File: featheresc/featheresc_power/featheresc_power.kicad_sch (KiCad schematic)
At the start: 19 parts, among them J1 VIN_GND, J2 VIN_POS, J7 interconnect1, J8 interconnect2

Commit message: Power board: update terminals, many minor tweaks
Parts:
- J1, J2: footprint featheresc:screw_lug_terminal -> featheresc:screwterminal_temile_MFR04425
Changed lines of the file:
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@@
     (date "2021-11-20")
   )
+  (junction (at 114.3 94.615) (diameter 0) (color 0 0 0 0))
+  (junction (at 110.49 76.835) (diameter 0) (color 0 0 0 0))
+  (junction (at 73.025 94.615) (diameter 0) (color 0 0 0 0))
   (junction (at 126.365 76.835) (diameter 0) (color 0 0 0 0))
-  (junction (at 122.555 76.835) (diameter 0) (color 0 0 0 0))
-  (junction (at 110.49 94.615) (diameter 0) (color 0 0 0 0))
+  (junction (at 109.22 101.6) (diameter 0) (color 0 0 0 0))
+  (junction (at 114.3 101.6) (diameter 0) (color 0 0 0 0))
+  (junction (at 122.555 58.42) (diameter 0) (color 0 0 0 0))
+  (junction (at 82.55 76.835) (diameter 0) (color 0 0 0 0))
   (junction (at 80.645 101.6) (diameter 0) (color 0 0 0 0))
   (junction (at 109.22 106.68) (diameter 0) (color 0 0 0 0))
-  (junction (at 114.3 101.6) (diameter 0) (color 0 0 0 0))
+  (junction (at 82.55 94.615) (diameter 0) (color 0 0 0 0))
+  (junction (at 82.55 58.42) (diameter 0) (color 0 0 0 0))
   (junction (at 80.645 106.68) (diameter 0) (color 0 0 0 0))
-  (junction (at 109.22 101.6) (diameter 0) (color 0 0 0 0))
-  (junction (at 82.55 94.615) (diameter 0) (color 0 0 0 0))
-  (junction (at 122.555 58.42) (diameter 0) (color 0 0 0 0))
-  (junction (at 114.3 94.615) (diameter 0) (color 0 0 0 0))
+  (junction (at 110.49 94.615) (diameter 0) (color 0 0 0 0))
   (junction (at 126.365 94.615) (diameter 0) (color 0 0 0 0))
   (junction (at 73.025 101.6) (diameter 0) (color 0 0 0 0))
-  (junction (at 110.49 76.835) (diameter 0) (color 0 0 0 0))
-  (junction (at 82.55 58.42) (diameter 0) (color 0 0 0 0))
-  (junction (at 82.55 76.835) (diameter 0) (color 0 0 0 0))
-  (junction (at 73.025 94.615) (diameter 0) (color 0 0 0 0))
+  (junction (at 122.555 76.835) (diameter 0) (color 0 0 0 0))
   (no_connect (at 142.24 133.35))
   (no_connect (at 178.435 133.35))
+  (wire (pts (xy 93.98 111.125) (xy 80.645 111.125))
+    (stroke (width 0) (type default) (color 0 0 0 0))
+  )
   (wire (pts (xy 80.645 111.125) (xy 80.645 106.68))
     (stroke (width 0) (type default) (color 0 0 0 0))
   )
-  (wire (pts (xy 93.98 111.125) (xy 80.645 111.125))
+  (wire (pts (xy 73.025 101.6) (xy 80.645 101.6))
     (stroke (width 0) (type default) (color 0 0 0 0))
   )
@@
     (stroke (width 0) (type default) (color 0 0 0 0))
   )
-  (wire (pts (xy 73.025 101.6) (xy 80.645 101.6))
-    (stroke (width 0) (type default) (color 0 0 0 0))
-  )
   (wire (pts (xy 191.135 114.935) (xy 191.135 133.35))
     (stroke (width 0) (type default) (color 0 0 0 0))
@@
     (stroke (width 0) (type default) (color 0 0 0 0))
   )
+  (wire (pts (xy 73.025 94.615) (xy 73.025 101.6))
+    (stroke (width 0) (type default) (color 0 0 0 0))
+  )
   (wire (pts (xy 73.025 121.92) (xy 120.65 121.92))
     (stroke (width 0) (type default) (color 0 0 0 0))
   )
-  (wire (pts (xy 73.025 94.615) (xy 73.025 101.6))
-    (stroke (width 0) (type default) (color 0 0 0 0))
-  )
   (wire (pts (xy 109.22 106.68) (xy 109.22 101.6))
     (stroke (width 0) (type default) (color 0 0 0 0))
@@
     (stroke (width 0) (type default) (color 0 0 0 0))
   )
+  (wire (pts (xy 114.3 94.615) (xy 126.365 94.615))
+    (stroke (width 0) (type default) (color 0 0 0 0))
+  )
+  (wire (pts (xy 126.365 94.615) (xy 138.43 94.615))
+    (stroke (width 0) (type default) (color 0 0 0 0))
+  )
   (wire (pts (xy 110.49 94.615) (xy 114.3 94.615))
     (stroke (width 0) (type default) (color 0 0 0 0))
   )
-  (wire (pts (xy 114.3 94.615) (xy 126.365 94.615))
-    (stroke (width 0) (type default) (color 0 0 0 0))
-  )
-  (wire (pts (xy 126.365 94.615) (xy 138.43 94.615))
-    (stroke (width 0) (type default) (color 0 0 0 0))
-  )
   (wire (pts (xy 92.71 88.9) (xy 92.71 94.615))
     (stroke (width 0) (type default) (color 0 0 0 0))
@@
     (stroke (width 0) (type default) (color 0 0 0 0))
   )
+  (wire (pts (xy 80.645 106.68) (xy 80.645 101.6))
+    (stroke (width 0) (type default) (color 0 0 0 0))
+  )
   (wire (pts (xy 93.98 106.68) (xy 80.645 106.68))
     (stroke (width 0) (type default) (color 0 0 0 0))
   )
-  (wire (pts (xy 80.645 106.68) (xy 80.645 101.6))
-    (stroke (width 0) (type default) (color 0 0 0 0))
-  )
   (wire (pts (xy 149.86 57.15) (xy 170.18 57.15))
     (stroke (width 0) (type default) (color 0 0 0 0))
@@
     (stroke (width 0) (type default) (color 0 0 0 0))
   )
+  (wire (pts (xy 82.55 58.42) (xy 122.555 58.42))
+    (stroke (width 0) (type default) (color 0 0 0 0))
+  )
   (wire (pts (xy 73.025 58.42) (xy 82.55 58.42))
     (stroke (width 0) (type default) (color 0 0 0 0))
   )
-  (wire (pts (xy 82.55 58.42) (xy 122.555 58.42))
-    (stroke (width 0) (type default) (color 0 0 0 0))
-  )
   (wire (pts (xy 62.23 80.645) (xy 73.025 80.645))
     (stroke (width 0) (type default) (color 0 0 0 0))
   )
+  (wire (pts (xy 122.555 76.835) (xy 126.365 76.835))
+    (stroke (width 0) (type default) (color 0 0 0 0))
+  )
   (wire (pts (xy 110.49 76.835) (xy 122.555 76.835))
     (stroke (width 0) (type default) (color 0 0 0 0))
   )
-  (wire (pts (xy 122.555 76.835) (xy 126.365 76.835))
-    (stroke (width 0) (type default) (color 0 0 0 0))
-  )
   (wire (pts (xy 139.7 133.35) (xy 139.7 130.175))
     (stroke (width 0) (type default) (color 0 0 0 0))
@@
     (stroke (width 0) (type default) (color 0 0 0 0))
   )
+  (wire (pts (xy 114.3 101.6) (xy 114.3 102.235))
+    (stroke (width 0) (type default) (color 0 0 0 0))
+  )
   (wire (pts (xy 114.3 94.615) (xy 114.3 101.6))
     (stroke (width 0) (type default) (color 0 0 0 0))
   )
-  (wire (pts (xy 114.3 101.6) (xy 114.3 102.235))
-    (stroke (width 0) (type default) (color 0 0 0 0))
-  )
   (wire (pts (xy 205.105 109.22) (xy 217.805 109.22))
     (stroke (width 0) (type default) (color 0 0 0 0))
@@
     (stroke (width 0) (type default) (color 0 0 0 0))
   )
+  (wire (pts (xy 138.43 76.835) (xy 126.365 76.835))
+    (stroke (width 0) (type default) (color 0 0 0 0))
+  )
   (wire (pts (xy 138.43 81.28) (xy 138.43 76.835))
     (stroke (width 0) (type default) (color 0 0 0 0))
   )
-  (wire (pts (xy 138.43 76.835) (xy 126.365 76.835))
+  (wire (pts (xy 101.6 101.6) (xy 109.22 101.6))
     (stroke (width 0) (type default) (color 0 0 0 0))
   )
   (wire (pts (xy 109.22 101.6) (xy 114.3 101.6))
-    (stroke (width 0) (type default) (color 0 0 0 0))
-  )
-  (wire (pts (xy 101.6 101.6) (xy 109.22 101.6))
     (stroke (width 0) (type default) (color 0 0 0 0))
   )
@@
     (property "Reference" "J2" (id 0) (at 54.5719 74.93 0))
     (property "Value" "VIN_POS" (id 1) (at 54.5719 77.47 0))
-    (property "Footprint" "featheresc:screw_lug_terminal" (id 2) (at 57.15 80.645 0)
+    (property "Footprint" "featheresc:screwterminal_temile_MFR04425" (id 2) (at 57.15 80.645 0)
       (effects (font (size 1.27 1.27)) hide)
     )
@@
     (property "Reference" "J1" (id 0) (at 55.2069 82.55 0))
     (property "Value" "VIN_GND" (id 1) (at 55.2069 85.09 0))
-    (property "Footprint" "featheresc:screw_lug_terminal" (id 2) (at 57.785 88.265 0)
+    (property "Footprint" "featheresc:screwterminal_temile_MFR04425" (id 2) (at 57.785 88.265 0)
       (effects (font (size 1.27 1.27)) hide)
     )
@@
     )
     (path "/7f2aeab9-ec9d-43c7-9eea-634b83a3de82"
-      (reference "J1") (unit 1) (value "VIN_GND") (footprint "featheresc:screw_lug_terminal")
+      (reference "J1") (unit 1) (value "VIN_GND") (footprint "featheresc:screwterminal_temile_MFR04425")
     )
     (path "/77203ab2-8235-47db-8b4e-3d9252007413"
-      (reference "J2") (unit 1) (value "VIN_POS") (footprint "featheresc:screw_lug_terminal")
+      (reference "J2") (unit 1) (value "VIN_POS") (footprint "featheresc:screwterminal_temile_MFR04425")
     )
     (path "/33d6cf7d-cc68-46b0-a73a-fd7eaf27dd2f/cd379072-4341-42c6-a956-8b88b065c937"
-      (reference "J3") (unit 1) (value "PHASE2") (footprint "featheresc:screw_lug_terminal")
+      (reference "J3") (unit 1) (value "PHASE2") (footprint "featheresc:screwterminal_temile_MFR04425")
     )
     (path "/33d6cf7d-cc68-46b0-a73a-fd7eaf27dd2f/39b11cc6-d366-44a2-83ef-19277836fb6b"
-      (reference "J4") (unit 1) (value "PHASE1") (footprint "featheresc:screw_lug_terminal")
+      (reference "J4") (unit 1) (value "PHASE1") (footprint "featheresc:screwterminal_temile_MFR04425")
     )
     (path "/a0a9a081-e3e0-435f-bc76-790ff1e001ff/cd379072-4341-42c6-a956-8b88b065c937"
-      (reference "J5") (unit 1) (value "PHASE2") (footprint "featheresc:screw_lug_terminal")
+      (reference "J5") (unit 1) (value "PHASE2") (footprint "featheresc:screwterminal_temile_MFR04425")
     )
     (path "/a0a9a081-e3e0-435f-bc76-790ff1e001ff/39b11cc6-d366-44a2-83ef-19277836fb6b"
-      (reference "J6") (unit 1) (value "PHASE1") (footprint "featheresc:screw_lug_terminal")
+      (reference "J6") (unit 1) (value "PHASE1") (footprint "featheresc:screwterminal_temile_MFR04425")
     )
     (path "/35384852-5afc-4c26-9852-40e0bc521a5e"

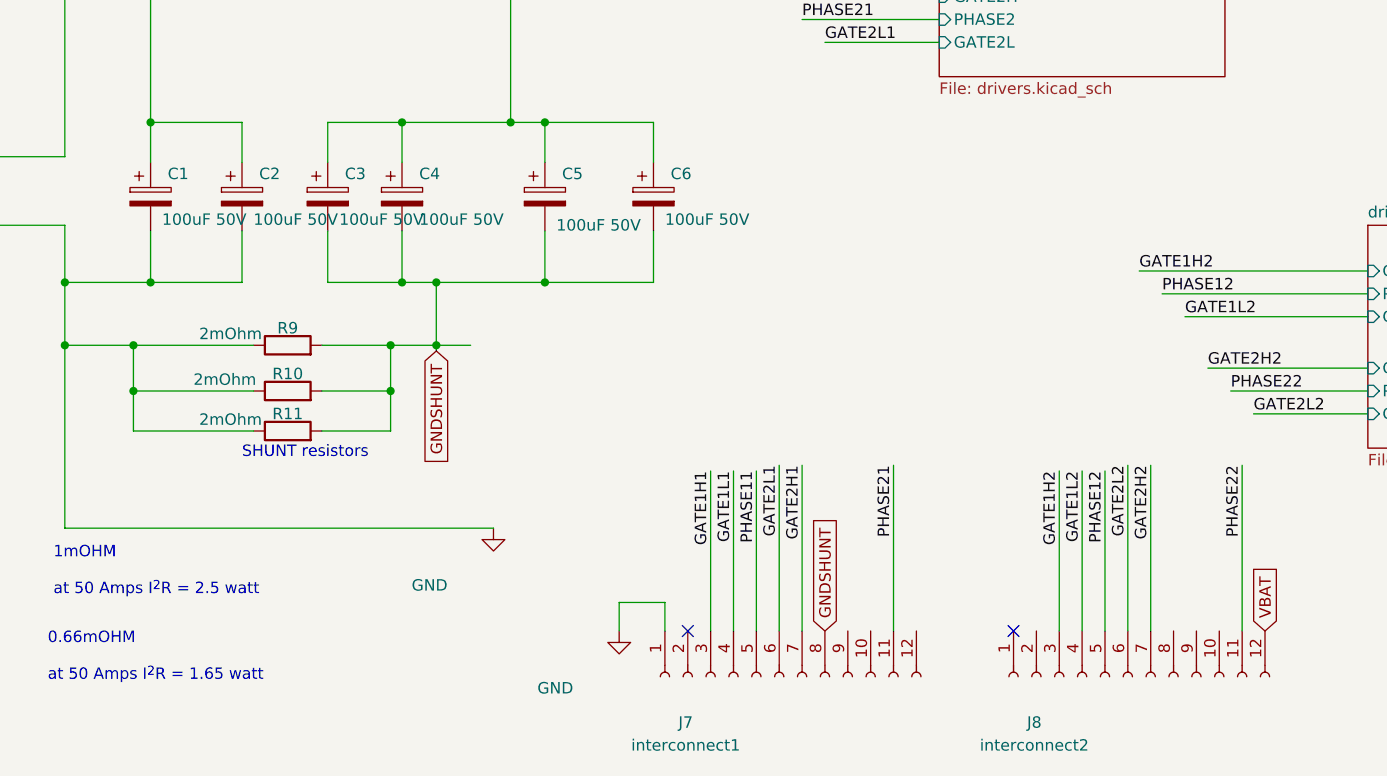
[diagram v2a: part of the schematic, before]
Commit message: Update layout to be more compact, swap a few parts
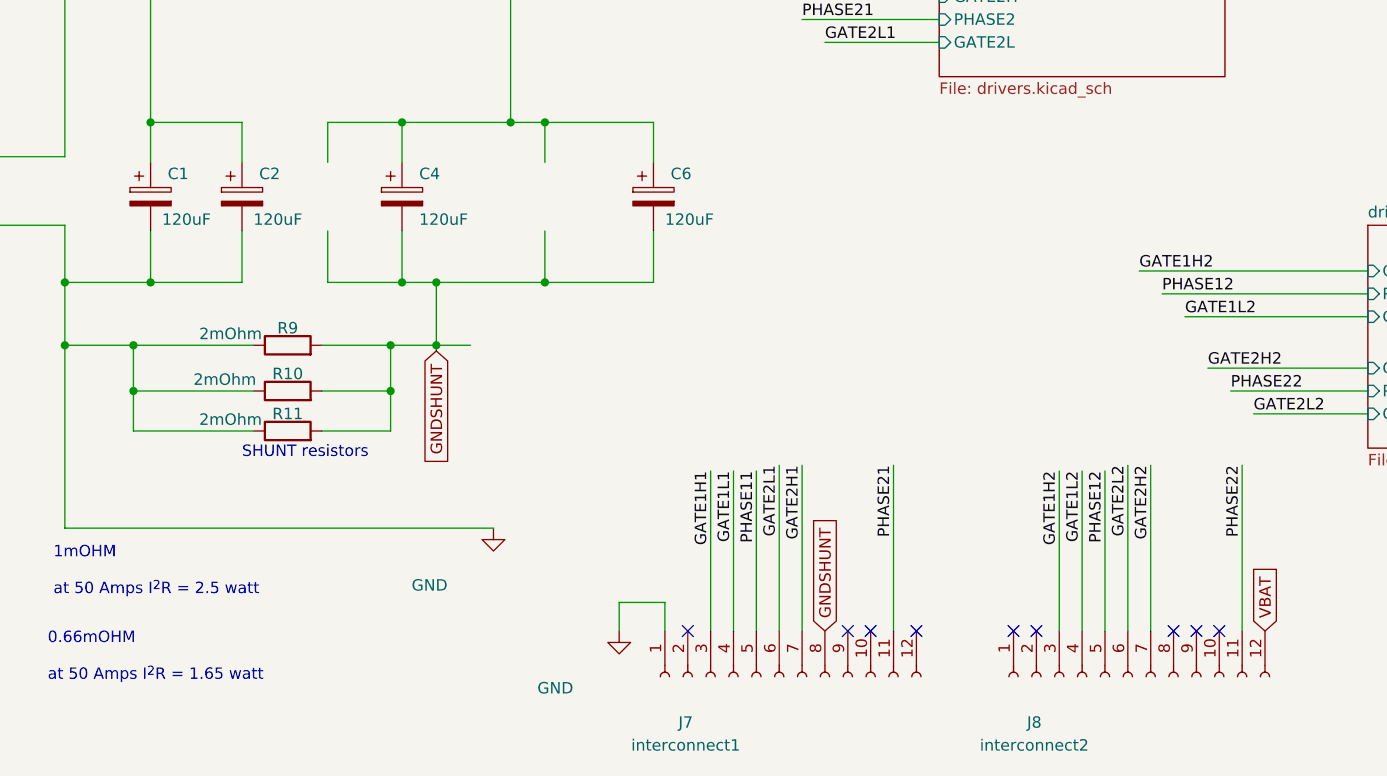
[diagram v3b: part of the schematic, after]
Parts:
- removed C3, C5: 100uF 50V, Capacitor_SMD:CP_Elec_8x10, symbol Device:C_Polarized
- C1, C2, C4, C6: value 100uF 50V -> 120uF; footprint Capacitor_SMD:CP_Elec_8x10 -> Capacitor_THT:CP_Radial_D10.0mm_P2.50mm_P5.00mm; MPN UUD1H101MNL1GS -> LKME0901J121MF; Manufacturer Nichicon -> Ymin
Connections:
- no-connect marks 2 -> 9
